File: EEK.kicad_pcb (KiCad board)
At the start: 2 copper layers, 165 x 51.8 mm, 36 parts

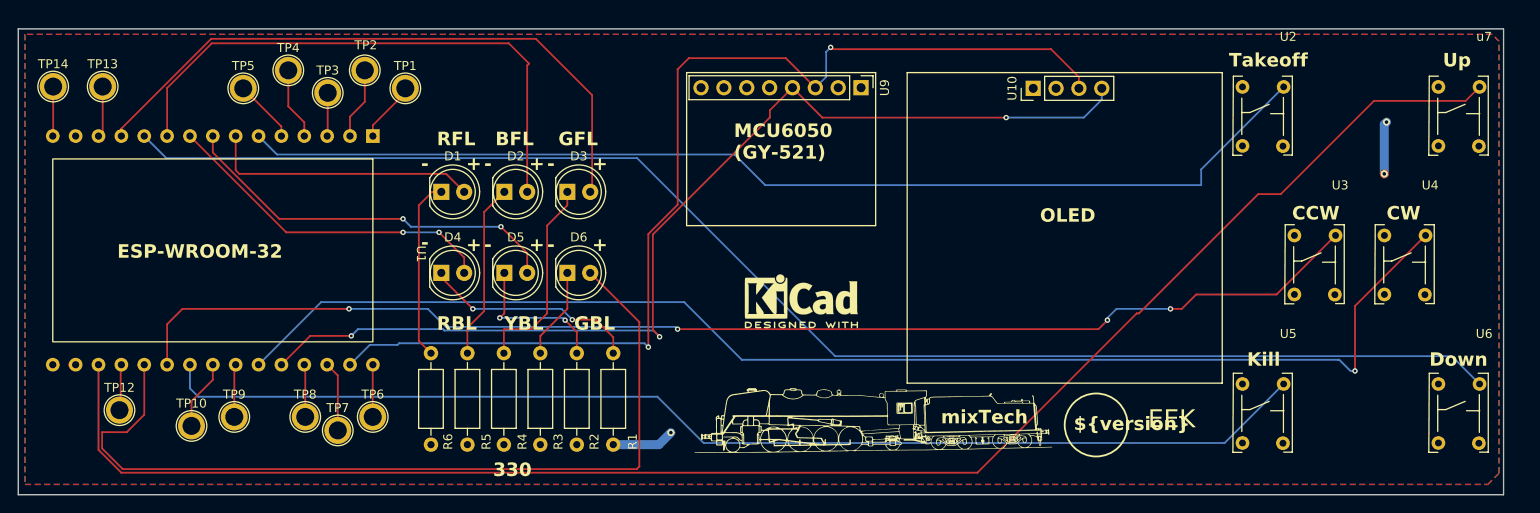
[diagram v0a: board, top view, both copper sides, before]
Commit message: Add exclusion zone for the antenna of the ESP32
Add exclusion zone for the antenna of the ESP32
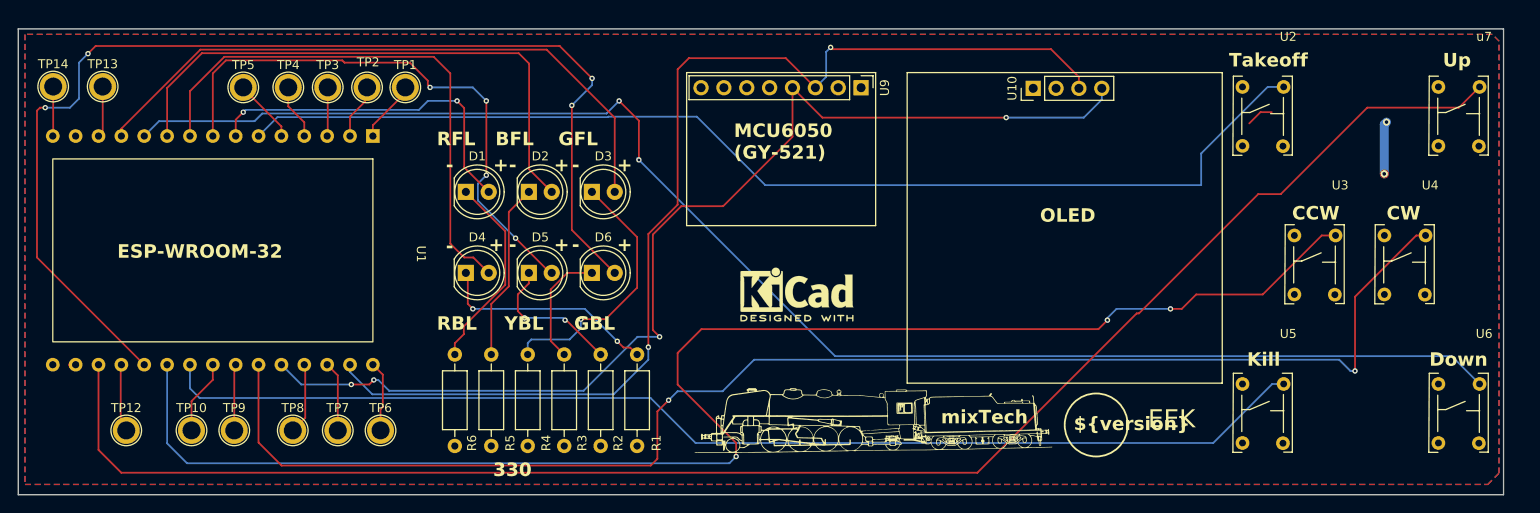
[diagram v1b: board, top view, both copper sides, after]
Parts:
- moved D1 2.72 mm to (92.2, 94.9)
- moved D2 2.72 mm to (99.2, 94.9)
- moved D3 2.72 mm to (106.2, 94.9)
- moved D4 2.72 mm to (92.2, 103.9)
- moved D5 2.72 mm to (99.2, 103.9)
- moved D6 2.72 mm to (106.2, 103.9)
- moved R1 2.65 mm to (111.2, 112.9)
- moved R2 2.65 mm to (107.2, 112.9)
- moved R3 2.65 mm to (103.2, 112.9)
- moved R6 2.65 mm to (91.0, 112.9)
- moved R4 2.65 mm to (99.1, 112.9)
- moved R5 2.65 mm to (95.0, 112.9)
- moved TP12 2.37 mm to (54.5, 121.4)
- moved TP8 2.04 mm to (73.0, 121.4)
- moved TP2 1.91 mm to (81.2, 83.2)
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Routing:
- net /GBL: track 97.4 -> 126.1 mm, vias 0 -> 4
- net /CCw: track 140.5 -> 166.1 mm, vias 4 -> 3
- net /RBR: track 38.0 -> 60.8 mm, vias 2 -> 0
- net /YBR: track 43.8 -> 63.1 mm, vias 2 -> 4
- net /CW: track 146.4 -> 159.1 mm, vias 1 -> 2
- net /GFL: track 30.2 -> 38.8 mm, vias 0 -> 2
- net Net-(D3-K): track 22.6 -> 29.6 mm, vias 0 -> 1
- net GND: track 13.5 -> 6.60 mm, vias 3 -> 2
- net /Down: track 159.7 -> 165.8 mm, vias 0 -> 2
- net /SDA: track 116.2 -> 121.1 mm, vias 3 -> 4
- net /SCL: track 119.1 -> 122.7 mm
- net (no net): track 0.00 -> 3.02 mm
- net Net-(D6-K): track 10.2 -> 13.2 mm
- net /Up: track 121.7 -> 124.5 mm
- net Net-(U1-ADC12_GPIO2): track 5.14 -> 7.59 mm
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
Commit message: Addvcapacitors for the switches and connector for battery
Add capacitors for the switches and connector for battery Vin
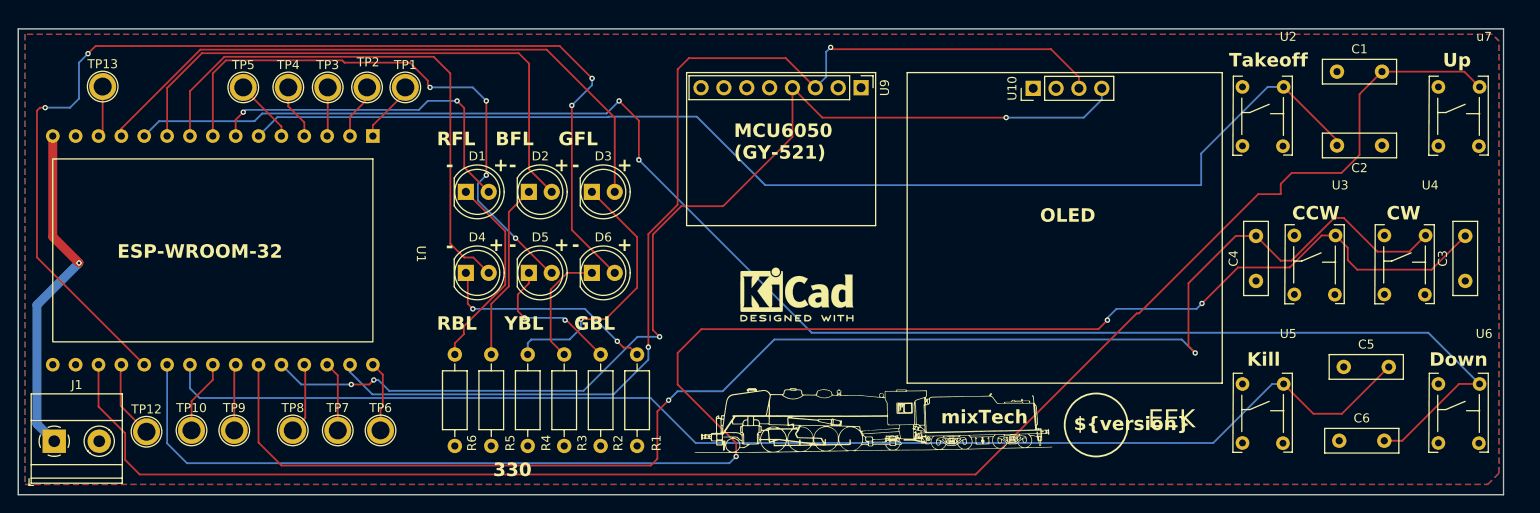
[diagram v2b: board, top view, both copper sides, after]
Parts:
- removed TP14: TestPoint, TestPoint:TestPoint_Plated_Hole_D2.0mm
- added C1: 0.1uf, Capacitor_THT:C_Disc_D8.0mm_W2.5mm_P5.00mm, F.Cu at (189.0, 81.5)
- added C2: 0.1uF, Capacitor_THT:C_Disc_D8.0mm_W2.5mm_P5.00mm, F.Cu at (194.0, 89.7)
- added C3: 0.1uF, Capacitor_THT:C_Disc_D8.0mm_W2.5mm_P5.00mm, F.Cu at (203.2, 104.8)
- added C4: 0.1uf, Capacitor_THT:C_Disc_D8.0mm_W2.5mm_P5.00mm, F.Cu at (180.0, 104.8)
- added C5: 0.1uf, Capacitor_THT:C_Disc_D8.0mm_W2.5mm_P5.00mm, F.Cu at (189.8, 114.3)
- added C6: 0.1uf, Capacitor_THT:C_Disc_D8.0mm_W2.5mm_P5.00mm, F.Cu at (189.2, 122.5)
- added J1: Screw_Terminal_01x02, TerminalBlock_Phoenix:TerminalBlock_Phoenix_MKDS-1,5-2_1x02_P5.00mm_Horizontal, F.Cu at (46.5, 122.6)
- moved TP12 2.25 mm to (56.8, 121.5)
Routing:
- net Net-(J1-Pin_1): track 5.52 -> 37.9 mm, vias 0 -> 1
- net /CCw: track 166.1 -> 184.5 mm
- net /Kill: track 129.4 -> 144.6 mm
- net /Down: track 165.8 -> 179.0 mm
- net /Up: track 124.5 -> 133.5 mm
- net /CW: track 159.1 -> 165.2 mm
- net GND: track 6.60 -> 0.72 mm, vias 2 -> 0
- net /Takeoff: track 181.7 -> 186.8 mm
- net (no net): track 3.02 -> 0.00 mm
- net Net-(U1-ADC12_GPIO2): track 7.59 -> 8.66 mm

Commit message: add footprint for oled with gnd on pin 1, improve the copper field
Add a second footprint for oled with the gnd on pin 1 instead pin 2. Improve the copper filed
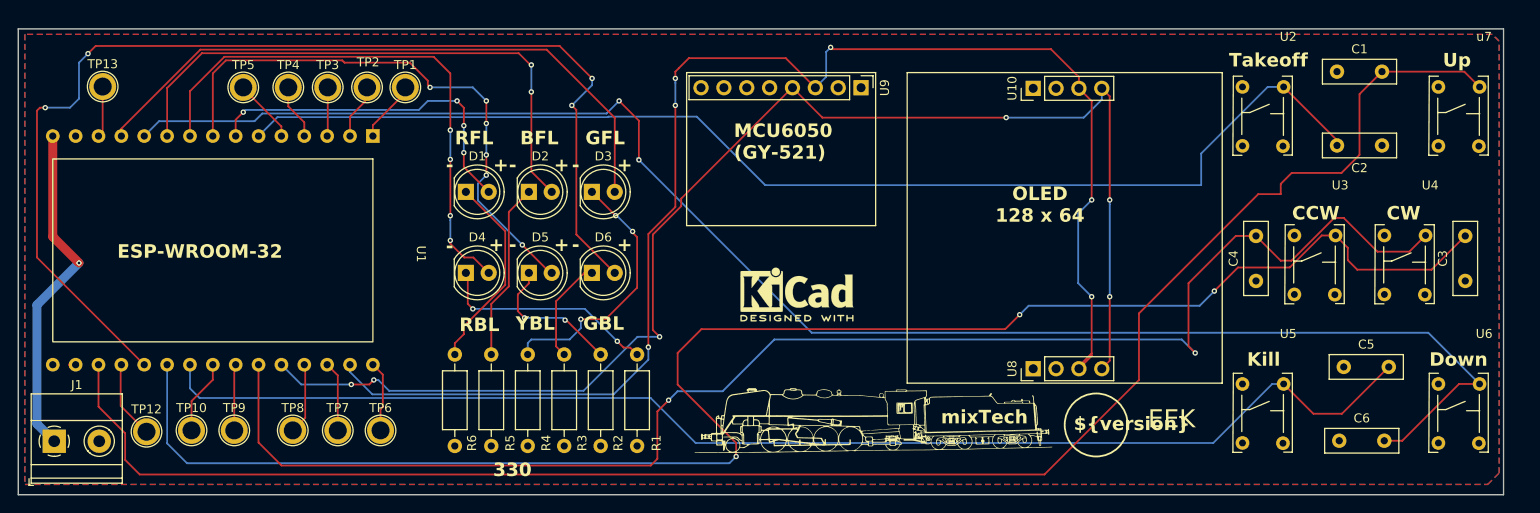
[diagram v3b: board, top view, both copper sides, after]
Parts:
- added U8: ~, Connector_PinHeader_2.54mm:PinHeader_1x04_P2.54mm_Vertical, F.Cu at (155.2, 114.5)
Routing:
- net /SCL: track 122.7 -> 158.5 mm, vias 2 -> 6
- net /SDA: track 121.1 -> 150.2 mm, vias 4 -> 6
- net /Takeoff: track 186.8 -> 191.1 mm
- net Net-(D6-K): track 13.2 -> 11.6 mm
- net Net-(D3-K): track 29.6 -> 29.8 mm, vias 1 -> 3
- net /BFL: track 62.9 -> 63.0 mm, vias 0 -> 2
- net /GFL: track 38.8 -> 38.9 mm, vias 2 -> 4
- net /YBR: vias 4 -> 6
- net /RBR: vias 0 -> 4
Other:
- board text added: "OLED 128 x 64"
- board text removed: "OLED"

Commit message: improve silkscreen, add capacitors on 3.3V, improve copper filed
improve silkscreen, add capacitors on 3.3V, improve copper filed
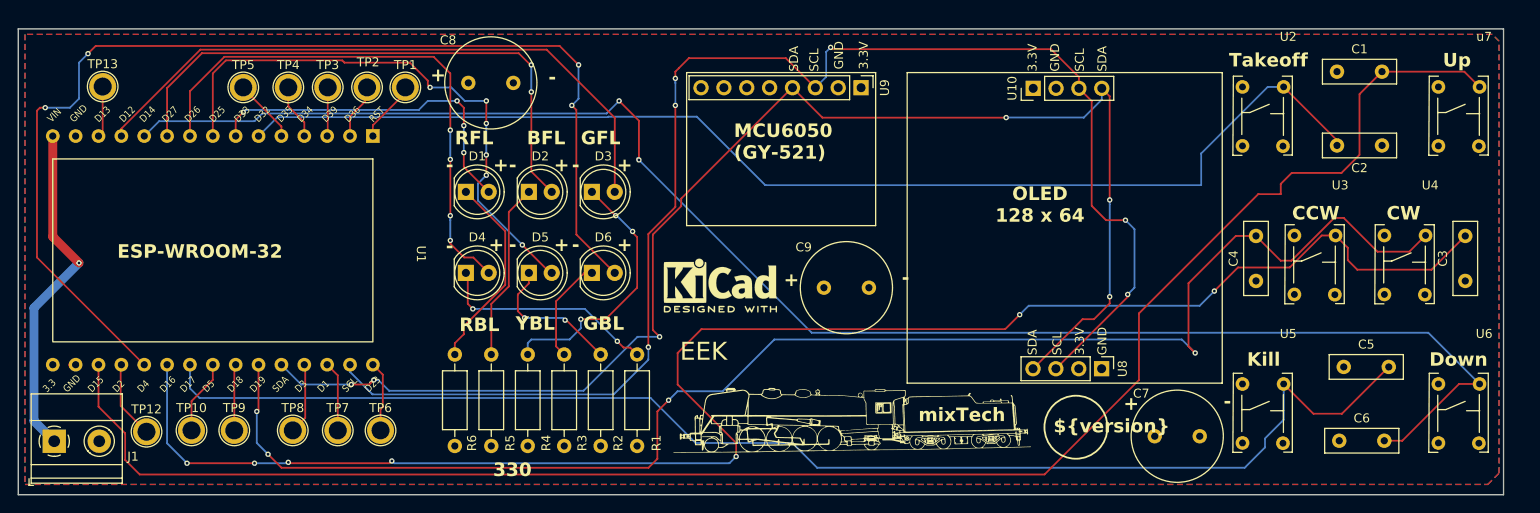
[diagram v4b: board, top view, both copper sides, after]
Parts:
- added C7: C, Capacitor_THT:C_Radial_D10.0mm_H12.5mm_P5.00mm, F.Cu at (168.8, 122.0)
- added C8: C, Capacitor_THT:C_Radial_D10.0mm_H12.5mm_P5.00mm, F.Cu at (92.5, 82.8)
- added C9: C, Capacitor_THT:C_Radial_D10.0mm_H12.5mm_P5.00mm, F.Cu at (132.0, 105.5)
- moved REF** 8.56 mm to (120.5, 105.2)
- moved U8 7.60 mm to (162.8, 114.5), turned to -90 degrees
- moved G*** 2.36 mm to (135.0, 119.8)
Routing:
- net /Kill: track 144.6 -> 149.7 mm
- net /SDA: track 150.2 -> 154.1 mm
- net /SCL: track 158.5 -> 161.3 mm
- net /GBL: track 126.1 -> 124.9 mm
- net /CW: track 165.2 -> 165.8 mm, vias 2 -> 4
- net /CCw: track 184.2 -> 184.5 mm, vias 3 -> 7
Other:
- board text added: "3.3"
- board text added: "3.3V"
- board text added: "D1"
- board text added: "D12"
- board text added: "D13"
- board text added: "D14"
- board text added: "D15"
- board text added: "D16"
- board text added: "D17"
- board text added: "D18"
- board text added: "D19"
- board text added: "D2"
- board text added: "D23"
- board text added: "D25"
- board text added: "D26"
- board text added: "D27"
- board text added: "D3"
- board text added: "D32"
- board text added: "D33"
- board text added: "D34"
- board text added: "D35"
- board text added: "D36"
- board text added: "D39"
- board text added: "D4"
- board text added: "D5"
- board text added: "GND"
- board text added: "RST"
- board text added: "SCL"
- board text added: "SDA"
- board text added: "VIN"

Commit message: copper filed and silkscreen  improvement
copper filed and silkscreen  improvement
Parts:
- moved C3 23.2 mm to (180.0, 104.8)
- moved C4 23.0 mm to (203.0, 104.8)
- moved U3 0.82 mm to (189.3, 93.8)
- moved U4 0.82 mm to (199.3, 93.8)
- moved C5 0.75 mm to (189.0, 114.3)
- moved C6 0.25 mm to (189.0, 122.5)
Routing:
- net /CCw: track 184.5 -> 168.2 mm
- net Net-(U1-GPIO35_ADC7): track 8.16 -> 11.7 mm, vias 0 -> 2
- net /CW: track 165.8 -> 168.3 mm
- net /Takeoff: track 191.1 -> 190.5 mm
- net /SDA: track 154.1 -> 154.7 mm
- net /YBR: track 63.1 -> 62.8 mm, vias 6 -> 10
- net /BFL: track 63.0 -> 62.8 mm, vias 2 -> 4
- net /RFL: track 70.6 -> 70.7 mm, vias 0 -> 2
- net /RBR: vias 4 -> 6

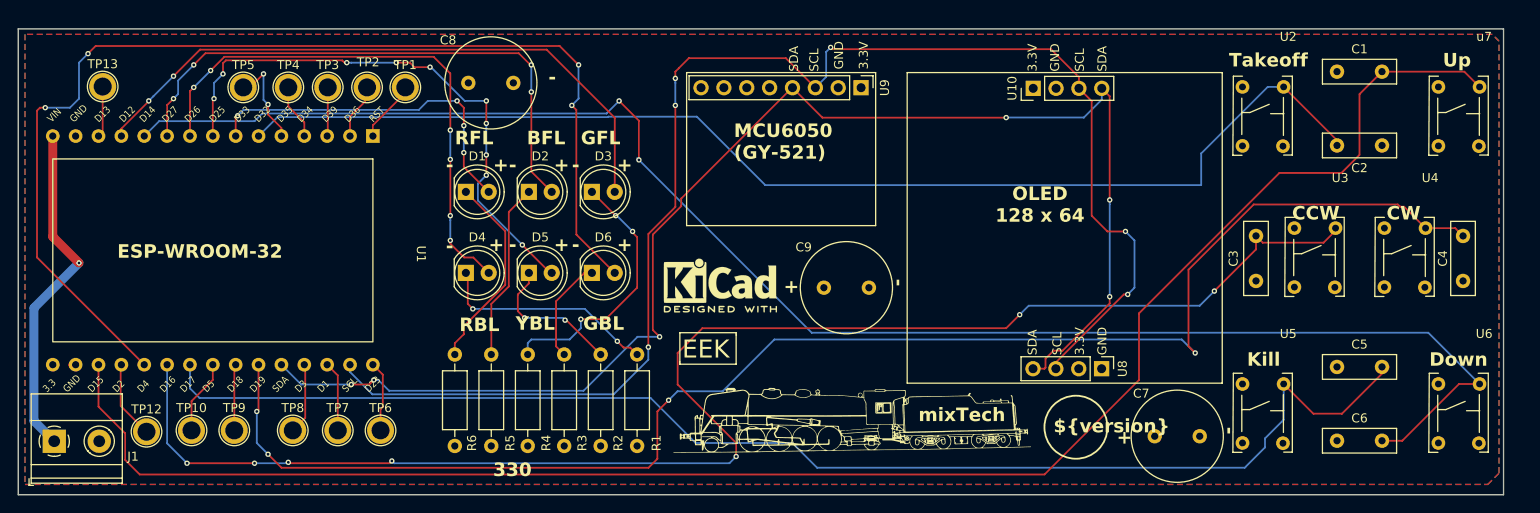
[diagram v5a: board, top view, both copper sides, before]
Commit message: add pull down 10K resistors on the switche
add pull down 10K resistors on the switche
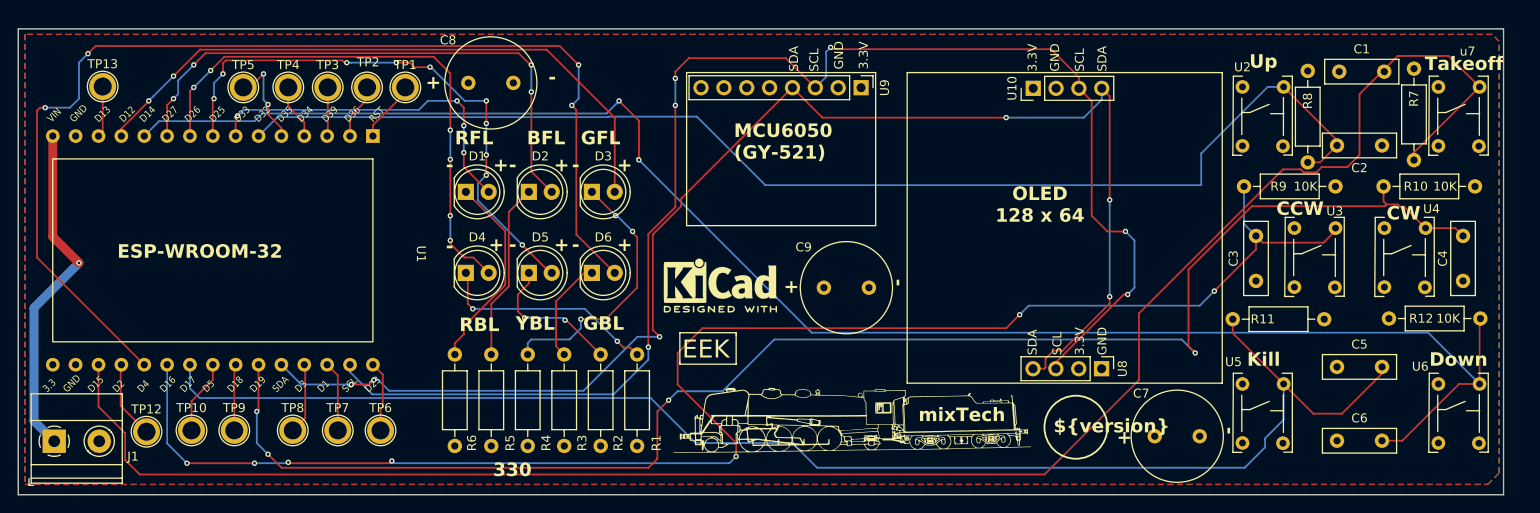
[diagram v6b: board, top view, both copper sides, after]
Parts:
- added R10: 10K, Resistor_THT:R_Axial_DIN0207_L6.3mm_D2.5mm_P10.16mm_Horizontal, F.Cu at (194.2, 94.2)
- added R11: 10K, Resistor_THT:R_Axial_DIN0207_L6.3mm_D2.5mm_P10.16mm_Horizontal, F.Cu at (177.4, 109.0)
- added R12: 10K, Resistor_THT:R_Axial_DIN0207_L6.3mm_D2.5mm_P10.16mm_Horizontal, F.Cu at (204.9, 108.9)
- added R7: 10K, Resistor_THT:R_Axial_DIN0207_L6.3mm_D2.5mm_P10.16mm_Horizontal, F.Cu at (197.6, 91.3)
- added R8: 10K, Resistor_THT:R_Axial_DIN0207_L6.3mm_D2.5mm_P10.16mm_Horizontal, F.Cu at (185.8, 91.6)
- added R9: 10K, Resistor_THT:R_Axial_DIN0207_L6.3mm_D2.5mm_P10.16mm_Horizontal, F.Cu at (178.7, 94.2)
- moved C1 0.25 mm to (189.2, 81.5)
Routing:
- net /Takeoff: track 190.5 -> 203.4 mm
- net /Kill: track 149.7 -> 159.3 mm
- net /Down: track 179.0 -> 186.3 mm
- net /CCw: track 168.2 -> 174.2 mm
- net /Up: track 133.5 -> 137.5 mm
- net /CW: track 168.3 -> 170.4 mm

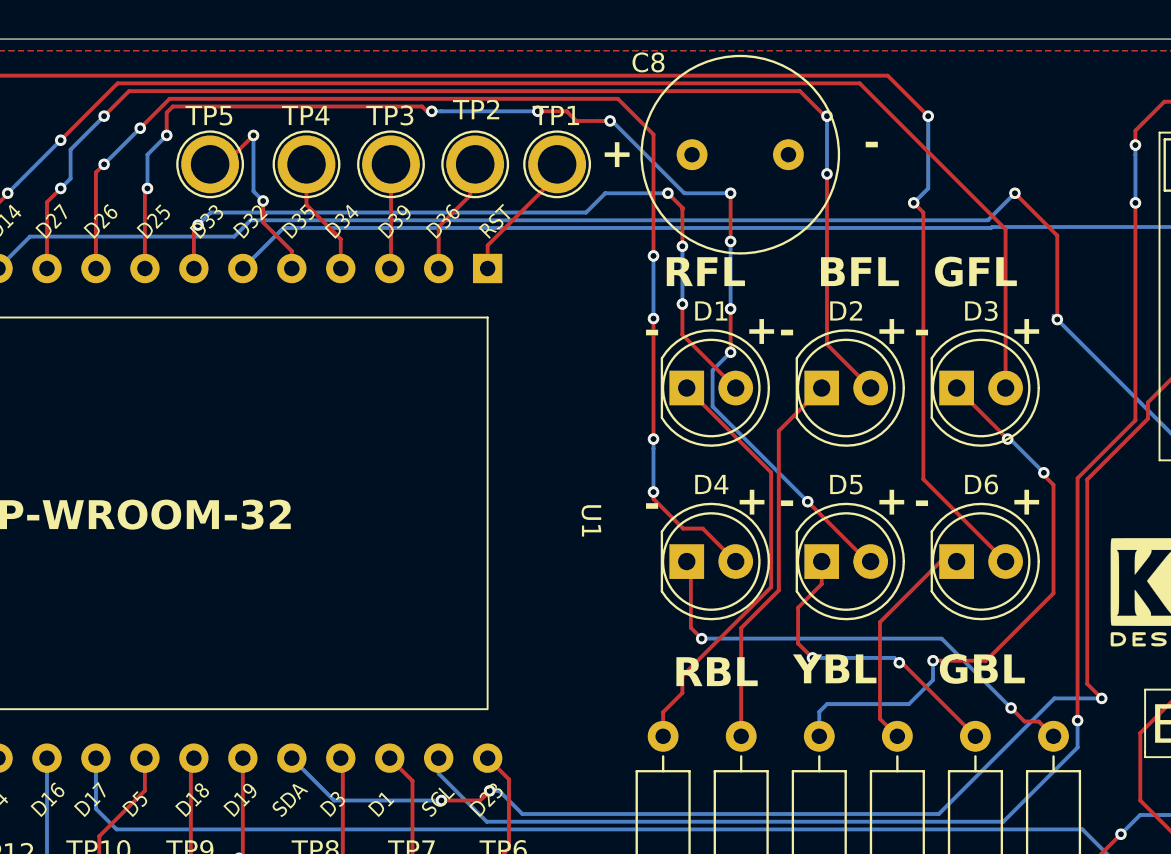
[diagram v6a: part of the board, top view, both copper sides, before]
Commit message: Invert LED D1 and LED D3
Invert LED D1 and LED D3
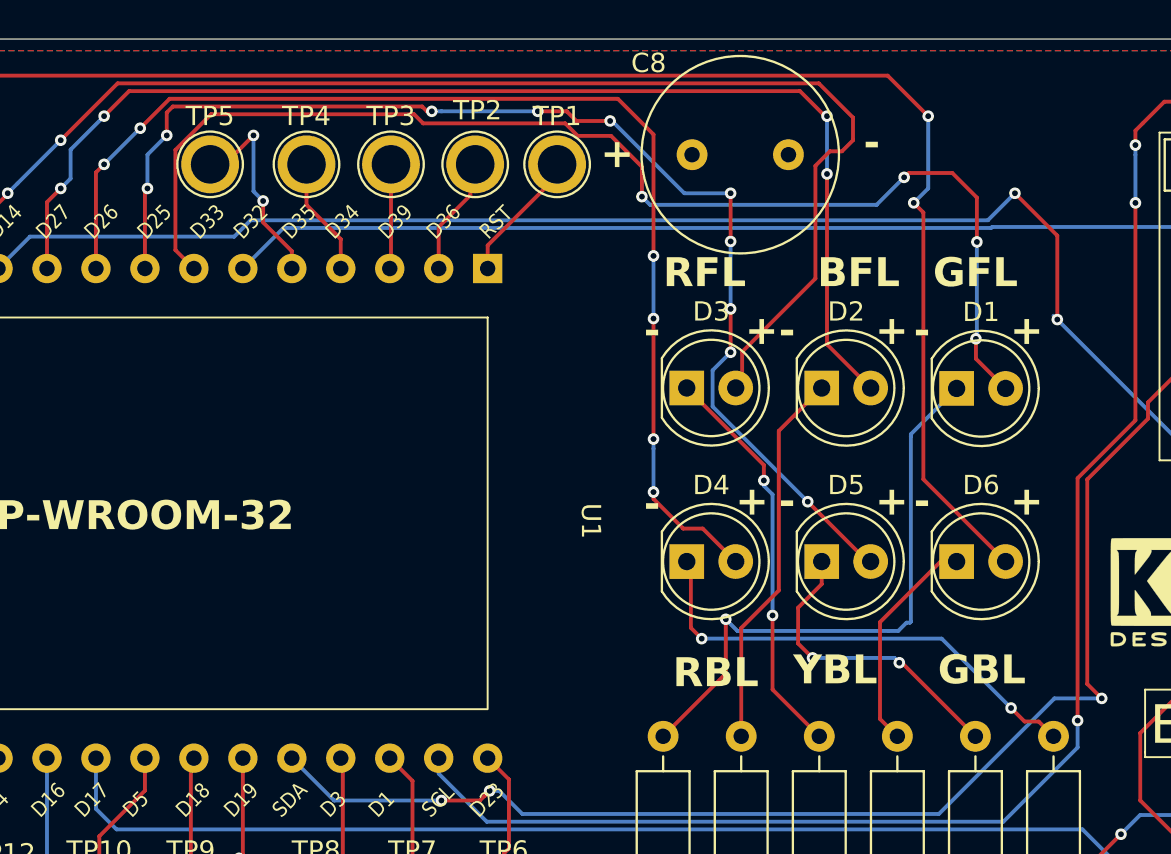
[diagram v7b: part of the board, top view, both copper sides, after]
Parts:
- moved D1 14.0 mm to (106.2, 94.9)
- moved D3 14.0 mm to (92.2, 94.8)
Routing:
- net /GFL: track 39.0 -> 63.5 mm
- net Net-(D3-K): track 29.8 -> 20.9 mm, vias 3 -> 2
- net Net-(D1-K): track 22.2 -> 30.5 mm, vias 0 -> 1
- net /RFL: track 70.7 -> 69.0 mm
